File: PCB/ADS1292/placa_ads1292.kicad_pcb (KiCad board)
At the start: 2 copper layers, 55 x 26.3 mm, 30 parts, among them P2 CONN_02X07, P3 CONN_01X04, P4 CONN_01X04, U2 REF5050, U3 ADS1292

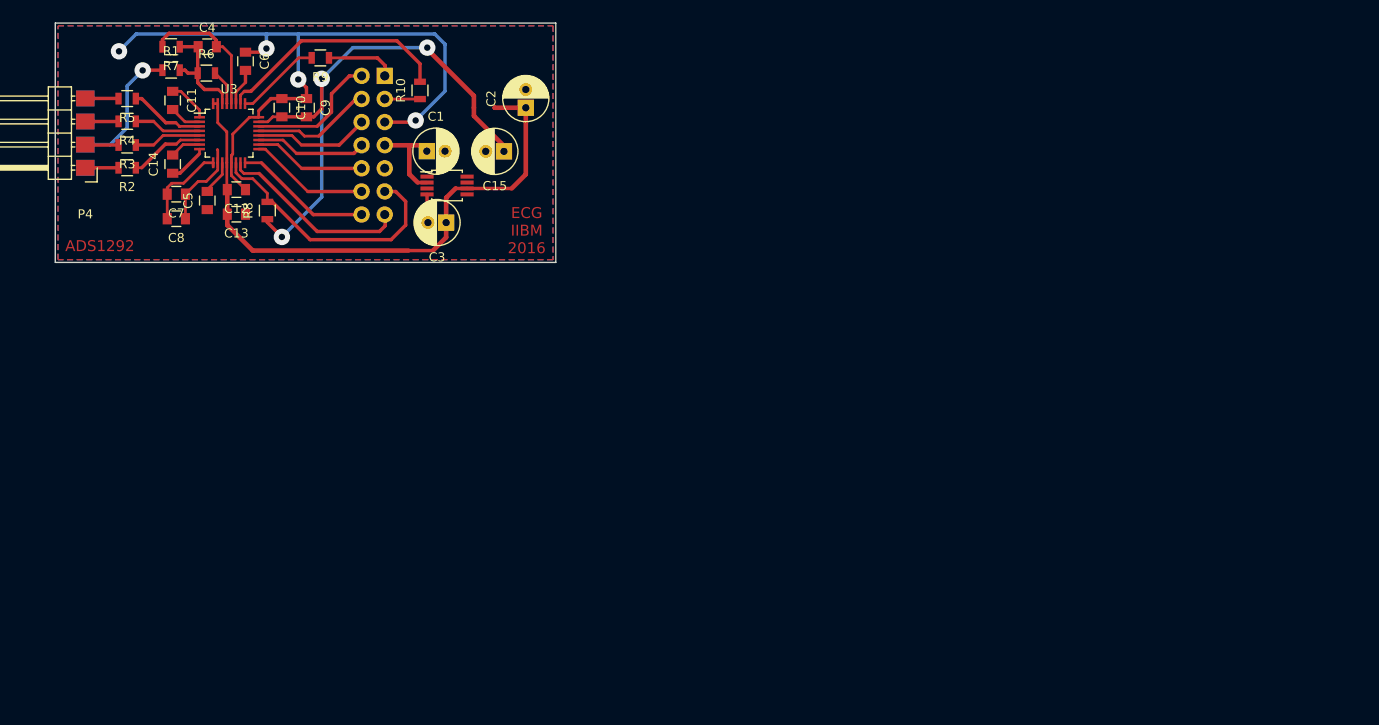
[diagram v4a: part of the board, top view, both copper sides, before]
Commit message: Modifico el PCB del ADS1292. Empiezo el pcb para el arduino.
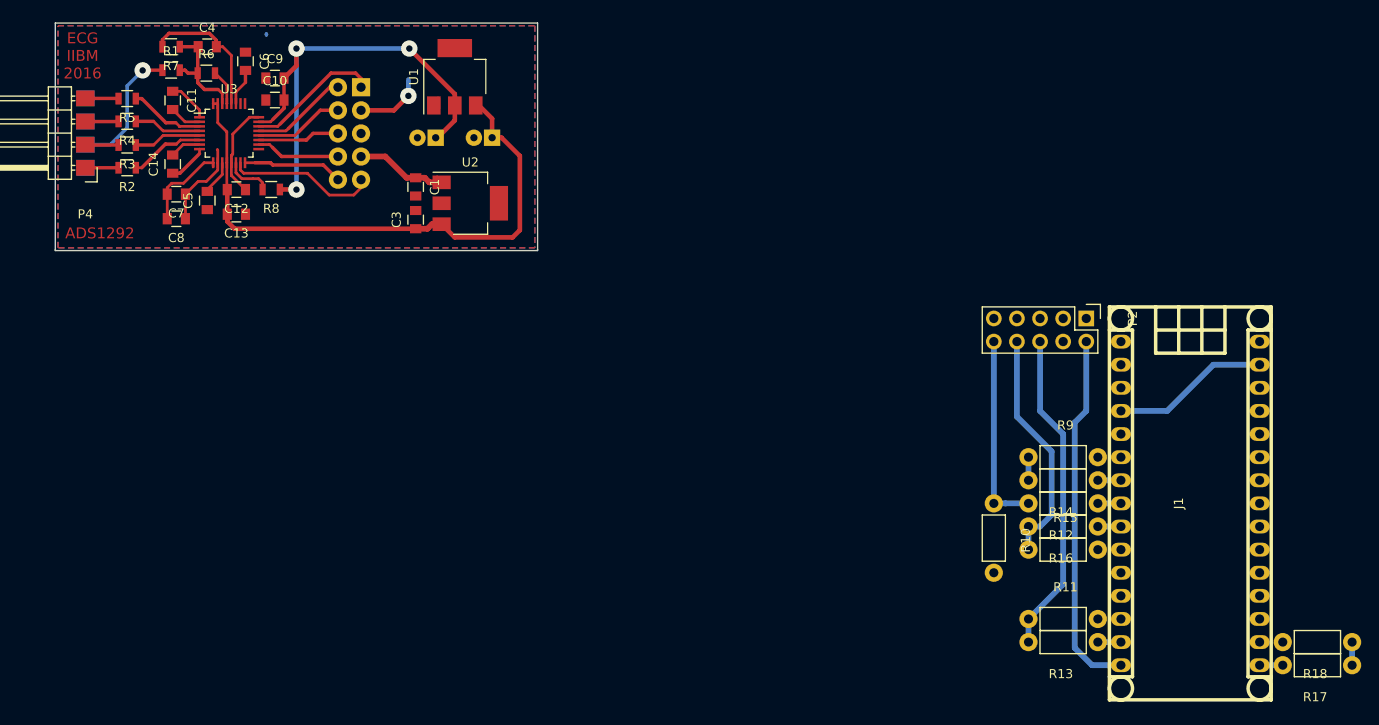
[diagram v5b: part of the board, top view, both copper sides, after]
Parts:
- added J1: Arduino_Nano_Header, w_conn_misc:arduino_nano_header, F.Cu at (223.5, 119.4)
- added P1: CONN_02X05, Connect:IDC_Header_Straight_10pins, B.Cu at (132.4, 73.7)
- added R11: 3k3, Resistors_ThroughHole:Resistor_Horizontal_RM7mm, F.Cu at (205.7, 132.1)
- added R12: 1k8, Resistors_ThroughHole:Resistor_Horizontal_RM7mm, F.Cu at (213.4, 119.4)
- added R13: 1k8, Resistors_ThroughHole:Resistor_Horizontal_RM7mm, F.Cu at (213.4, 134.6)
- added R14: 1k8, Resistors_ThroughHole:Resistor_Horizontal_RM7mm, F.Cu at (213.4, 116.8)
- added R15: 3k3, Resistors_ThroughHole:Resistor_Horizontal_RM7mm, F.Cu at (205.7, 124.5)
- added R16: 1k8, Resistors_ThroughHole:Resistor_Horizontal_RM7mm, F.Cu at (213.4, 121.9)
- added R17: 1k8, Resistors_ThroughHole:Resistor_Horizontal_RM7mm, F.Cu at (241.3, 137.2)
- added R18: 3k3, Resistors_ThroughHole:Resistor_Horizontal_RM7mm, F.Cu at (241.3, 134.6)
- added U1: AIC1117-33, TO_SOT_Packages_SMD:SOT-223, F.Cu at (142.7, 72.5)
- C1: value 1u -> 220nF; footprint Capacitors_ThroughHole:C_Radial_D5_L11_P2 -> Capacitors_SMD:C_0805
- C15, C2: moved to B.Cu
- C3: value 1u -> 100nF; footprint Capacitors_ThroughHole:C_Radial_D5_L11_P2 -> Capacitors_SMD:C_0805
- P2: value CONN_02X07 -> CONN_02X05; footprint Pin_Headers:Pin_Header_Straight_2x07 -> Pin_Headers:Pin_Header_Straight_2x05; moved to F.Cu
- R10, R9: value 10k -> 3k3; footprint Resistors_SMD:R_0805 -> Resistors_ThroughHole:Resistor_Horizontal_RM7mm
- U2: value REF5050 -> LM7805CT; footprint Housings_SSOP:MSOP-8_3x3mm_Pitch0.65mm -> TO_SOT_Packages_SMD:SOT-223
- moved R9 89.3 mm to (205.7, 114.3), turned to 0 degrees
- moved P2 81.6 mm to (212.1, 99.1), turned to 270 degrees
- moved R10 77.7 mm to (201.9, 119.4), turned to 270 degrees
- moved C15 7.65 mm to (140.6, 79.2)
- moved C2 4.96 mm to (146.8, 79.2), turned to 180 degrees
- moved C9 4.75 mm to (122.9, 72.6), turned to 0 degrees
- moved C1 4.11 mm to (138.4, 84.6), turned to 270 degrees
- moved C3 3.37 mm to (138.4, 88.2), turned to 90 degrees
- moved U2 3.21 mm to (144.4, 86.4)
- moved R8 2.35 mm to (122.5, 84.9), turned to 180 degrees
- moved C10 1.14 mm to (122.9, 75.1), turned to 0 degrees
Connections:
- P2 pad 1: Net-(P2-Pad1) -> /Arduino/DRDY
- P2 pad 10: Net-(P2-Pad10) -> /Arduino/START
- P2 pad 2: Net-(P2-Pad2) -> /Arduino/MISO
- P2 pad 3: Net-(P2-Pad3) -> GND
- P2 pad 4: Net-(P2-Pad4) -> /Arduino/SCK
- P2 pad 5: GND -> Net-(P2-Pad5)
- P2 pad 6: Net-(P2-Pad6) -> /Arduino/MOSI
- P2 pad 8: Net-(P2-Pad8) -> /Arduino/CS
- P2 pad 9: Net-(P2-Pad9) -> /Arduino/RESET
- R10 pad 1: Net-(P2-Pad3) -> /Arduino/START
- R10 pad 2: Net-(R10-Pad2) -> GND
- R8 pad 2: Net-(P2-Pad11) -> Net-(R8-Pad2)
- R9 pad 1: Net-(P2-Pad1) -> /Arduino/RESET
- R9 pad 2: Net-(R9-Pad2) -> GND
- U2 pad 1: (no net) -> +BATT
- U2 pad 2: +BATT -> GND
- U2 pad 3: Net-(U2-Pad3) -> +5V
- U3 pad 14: Net-(P2-Pad11) -> Net-(R8-Pad2)
- U3 pad 15: Net-(P2-Pad13) -> Net-(P1-Pad9)
- U3 pad 16: Net-(P2-Pad14) -> Net-(P1-Pad10)
- U3 pad 17: Net-(P2-Pad12) -> Net-(U3-Pad17)
- U3 pad 18: Net-(P2-Pad10) -> Net-(P1-Pad8)
- U3 pad 19: Net-(P2-Pad8) -> Net-(P1-Pad6)
- U3 pad 20: Net-(P2-Pad6) -> Net-(P1-Pad4)
- U3 pad 21: Net-(P2-Pad4) -> Net-(P1-Pad2)
- U3 pad 22: Net-(P2-Pad2) -> Net-(P1-Pad1)
- U3 pad 25: Net-(R9-Pad2) -> Net-(U3-Pad25)
- U3 pad 26: Net-(R10-Pad2) -> Net-(U3-Pad26)
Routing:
- net GND: track 91.6 -> 46.1 mm, vias 4 -> 1
- net /Arduino/MISO: track 0.00 -> 40.1 mm
- net /Arduino/MOSI: track 0.00 -> 35.7 mm
- net Net-(P2-Pad11): track 29.3 -> 0.00 mm
- net /Arduino/CS: track 0.00 -> 26.2 mm
- net Net-(R10-Pad2): track 26.1 -> 0.00 mm
- net /Arduino/START: track 0.00 -> 21.6 mm
- net Net-(P2-Pad13): track 21.0 -> 0.00 mm
- net Net-(P1-Pad9): track 0.00 -> 16.4 mm
- net Net-(P2-Pad14): track 15.2 -> 0.00 mm
- net Net-(P1-Pad1): track 0.00 -> 14.9 mm
- net Net-(P2-Pad2): track 14.8 -> 0.00 mm
- net Net-(P2-Pad12): track 13.3 -> 0.00 mm
- net Net-(P2-Pad4): track 13.3 -> 0.00 mm
- net Net-(P1-Pad10): track 0.00 -> 13.0 mm
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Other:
- board size 55 x 26.3 mm -> 53 x 25 mm

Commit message: Termino con el nuevo pcb del ADS1292 y del arduino
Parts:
- added P5: CONN_01X02, Sockets_MOLEX_KK-System:Socket_MOLEX-KK-RM3-96mm_Lock_2pin_straight, F.Cu at (109.5, 112.9)
- C1: value 220nF -> 330nF
- U2: footprint TO_SOT_Packages_SMD:SOT-223 -> TO_SOT_Packages_SMD:TO-252-2Lead
- moved R18 113.3 mm to (128.3, 142.9)
- moved R17 103.0 mm to (138.4, 142.9), turned to 0 degrees
- moved R11 87.7 mm to (118.1, 135.3), turned to 270 degrees
- moved P2 85.2 mm to (127.0, 104.1)
- moved J1 85.1 mm to (138.4, 120.0)
- moved R10 85.1 mm to (116.8, 120.0)
- moved R12 85.1 mm to (128.3, 120.0)
- moved R13 85.1 mm to (128.3, 135.3)
- moved R14 85.1 mm to (128.3, 117.5)
- moved R15 85.1 mm to (120.7, 125.1), turned to 270 degrees
- moved R16 85.1 mm to (128.3, 122.6)
- moved R9 85.1 mm to (120.7, 114.9)
- moved U2 14.6 mm to (141.1, 72.2), turned to 270 degrees
- moved C3 14.2 mm to (137.9, 74.0)
- moved C1 14.2 mm to (137.9, 70.4)
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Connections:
- P1 pad 3: GND -> +BATT
- P1 pad 7: +BATT -> GND
- P2 pad 3: GND -> +BATT
- P2 pad 7: +BATT -> GND
- P3 pad 1: Net-(P3-Pad1) -> GND
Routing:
- net /Arduino/SCK: track 2.54 -> 47.9 mm
- net +BATT: track 11.4 -> 43.3 mm
- net /Arduino/DRDY: track 0.00 -> 24.3 mm
- net GND: track 46.1 -> 22.6 mm, vias 1 -> 0
- net /Arduino/RESET: track 2.54 -> 20.6 mm, vias 0 -> 2
- net +5V: track 64.7 -> 74.8 mm
- net +3V3: track 56.2 -> 50.3 mm, vias 3 -> 2
- net /Arduino/CS: track 26.2 -> 20.9 mm
- net /Arduino/MISO: track 40.1 -> 35.1 mm
- net /Arduino/START: track 21.6 -> 17.1 mm
- net Net-(J1-Pad16): track 2.54 -> 5.08 mm
- net (no net): track 0.20 -> 1.92 mm
- net /Arduino/MOSI: track 35.7 -> 34.3 mm
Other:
- board size 53 x 25 mm -> 55 x 79.3 mm

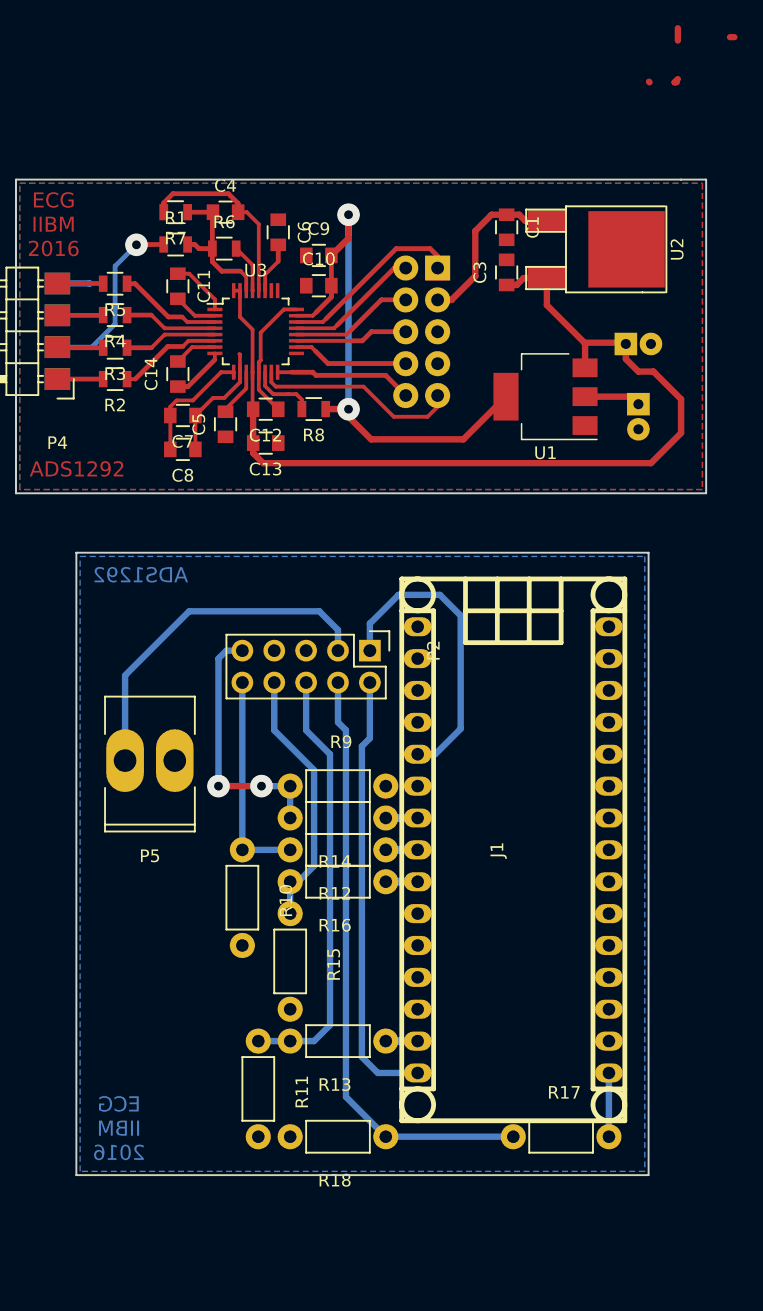
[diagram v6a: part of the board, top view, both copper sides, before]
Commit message: Agrando el pad de 3.3V del regulador. Cambio el footprint del arduino
para poner tiras de pines dobles. Agrego agujeros a la placa del arduino
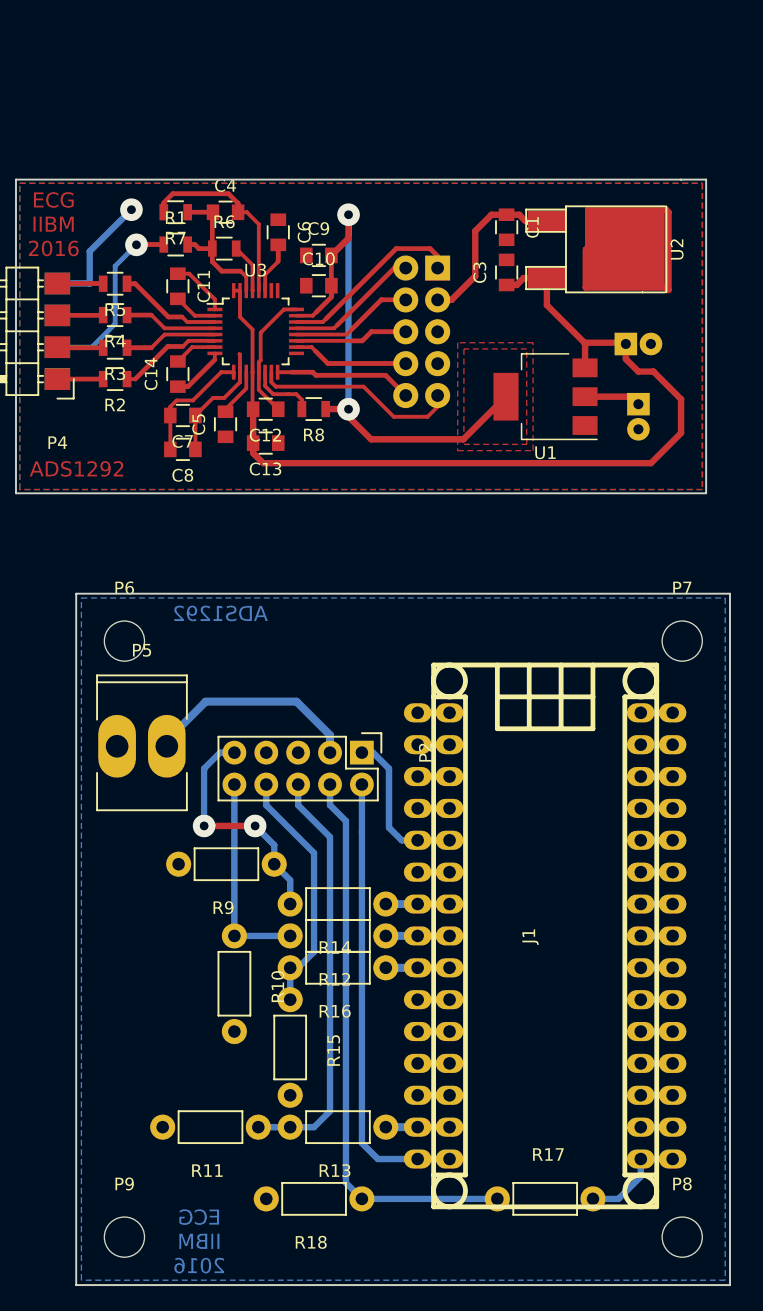
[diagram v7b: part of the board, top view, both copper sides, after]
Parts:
- added P6: CONN_01X01, Mounting_Holes:MountingHole_3.2mm_M3, F.Cu at (107.4, 103.4)
- added P7: CONN_01X01, Mounting_Holes:MountingHole_3.2mm_M3, F.Cu at (151.9, 103.4)
- added P8: CONN_01X01, Mounting_Holes:MountingHole_3.2mm_M3, F.Cu at (151.9, 150.9)
- added P9: CONN_01X01, Mounting_Holes:MountingHole_3.2mm_M3, F.Cu at (107.4, 150.9)
- moved P2 8.15 mm to (126.4, 112.3)
- moved J1 7.31 mm to (141.0, 126.9)
- moved R10 6.89 mm to (116.2, 126.9)
- moved R11 6.86 mm to (118.1, 142.1), turned to 180 degrees
- moved R12 6.86 mm to (128.3, 126.9)
- moved R13 6.86 mm to (128.3, 142.1)
- moved R14 6.86 mm to (128.3, 124.3)
- moved R15 6.86 mm to (120.7, 132.0)
- moved R16 6.86 mm to (128.3, 129.4)
- moved R9 6.35 mm to (119.4, 121.2), turned to 180 degrees
- moved R18 5.31 mm to (126.4, 147.8)
- moved R17 5.11 mm to (137.2, 147.8)
- moved P5 1.31 mm to (108.8, 111.8), turned to 0 degrees
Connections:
- P1 pad 5: Net-(P1-Pad5) -> GND
- P1 pad 7: GND -> Net-(P1-Pad7)
- P2 pad 5: Net-(P2-Pad5) -> GND
- P2 pad 7: GND -> Net-(P2-Pad7)
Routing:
- net GND: track 22.6 -> 61.8 mm, vias 0 -> 1
- net /Arduino/DRDY: track 24.3 -> 12.6 mm
- net +BATT: track 43.3 -> 32.5 mm
- net Net-(J1-Pad16): track 5.08 -> 8.48 mm
- net /Arduino/SCK: track 47.9 -> 44.9 mm
- net Net-(J1-Pad9): track 2.54 -> 5.08 mm
- net Net-(J1-Pad8): track 2.54 -> 5.08 mm
- net Net-(J1-Pad7): track 2.54 -> 5.08 mm
- net Net-(J1-Pad6): track 0.00 -> 2.54 mm
- net Net-(J1-Pad30): track 0.00 -> 2.54 mm
- net Net-(J1-Pad3): track 0.00 -> 2.54 mm
- net Net-(J1-Pad28): track 0.00 -> 2.54 mm
- net Net-(J1-Pad27): track 0.00 -> 2.54 mm
- net Net-(J1-Pad26): track 0.00 -> 2.54 mm
- net Net-(J1-Pad25): track 0.00 -> 2.54 mm
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- added copper zone on F.Cu, net +3V3
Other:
- board size 55 x 79.3 mm -> 56.9 x 88.1 mm

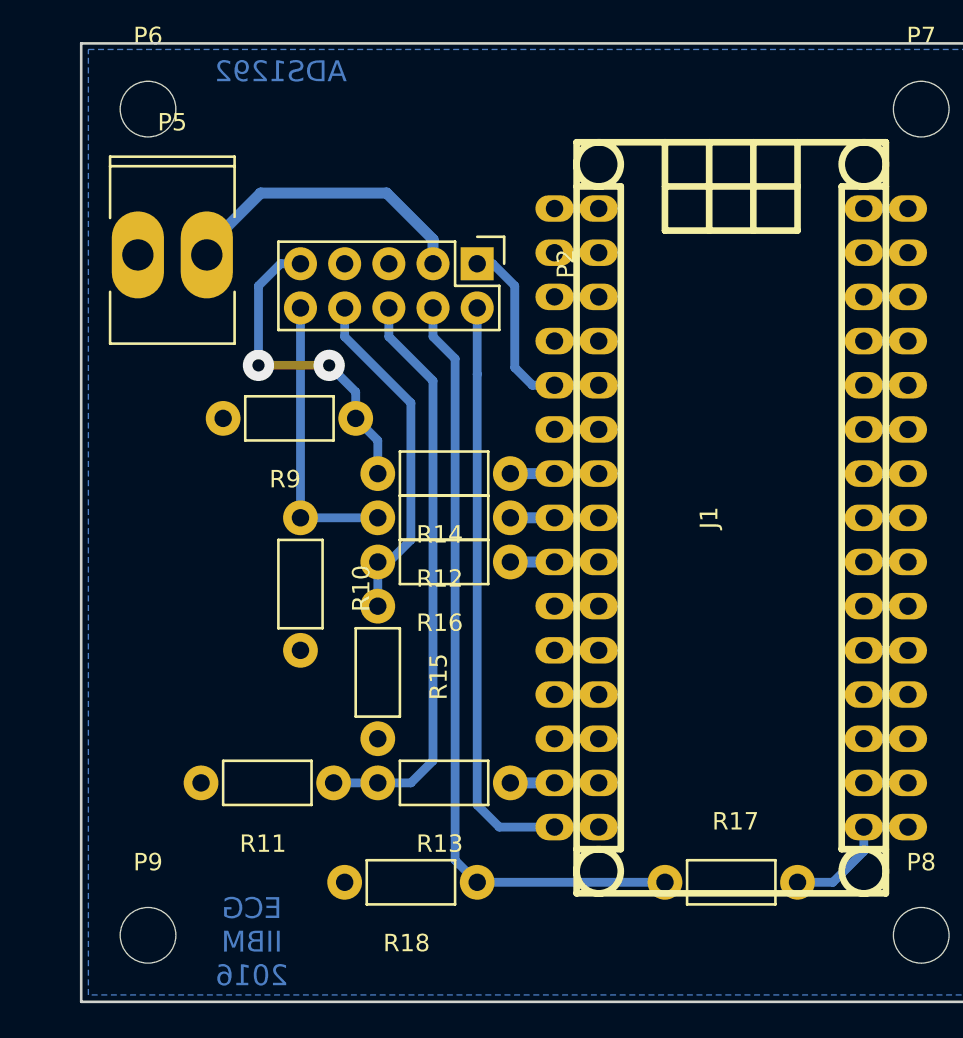
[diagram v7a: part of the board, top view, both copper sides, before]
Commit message: Nueva placa para el ADS1292 y el arduino. Cabezal modificado para
incorporar los electrodos de GND
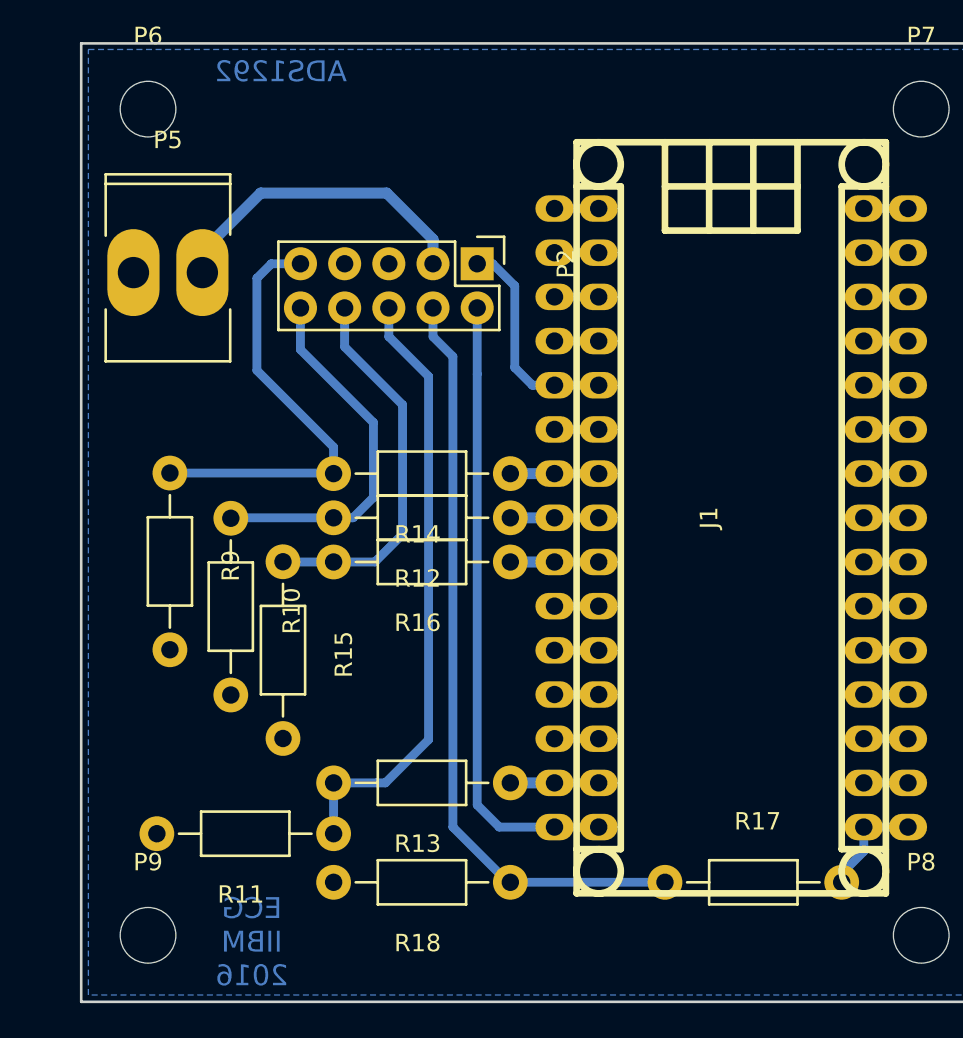
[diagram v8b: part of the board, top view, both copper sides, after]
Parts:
- R10, R11, R12, R13, R14, R15, R16, R17, R18, R9: footprint Resistors_ThroughHole:Resistor_Horizontal_RM7mm -> Resistors_ThroughHole:Resistor_Horizontal_RM10mm
- moved R9 11.1 mm to (108.7, 124.3), turned to 270 degrees
- moved R15 6.02 mm to (115.2, 129.4)
- moved R10 4.01 mm to (112.2, 126.9)
- moved R11 2.92 mm to (118.1, 145.0)
- moved R18 1.91 mm to (128.3, 147.8)
- moved P5 1.05 mm to (108.6, 112.8)
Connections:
- P2 pad 7: Net-(P2-Pad7) -> GND
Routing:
- net /Arduino/RESET: track 19.0 -> 25.3 mm, vias 2 -> 0
- net /Arduino/START: track 16.5 -> 21.3 mm
- net /Arduino/CS: track 19.9 -> 21.9 mm
- net Net-(J1-Pad16): track 8.48 -> 6.45 mm
- net /Arduino/MOSI: track 33.3 -> 35.2 mm
- net /Arduino/SCK: track 44.9 -> 43.8 mm
